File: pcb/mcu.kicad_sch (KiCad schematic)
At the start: 29 parts, among them SW3 TS04-66-50-BK-160-SMT, SW4 PTS645VH58-2 LFS, U1 W25Q128JVS, U2 RP2040, Y1 ABM8AIG-12.000MHZ-12-2Z-T3

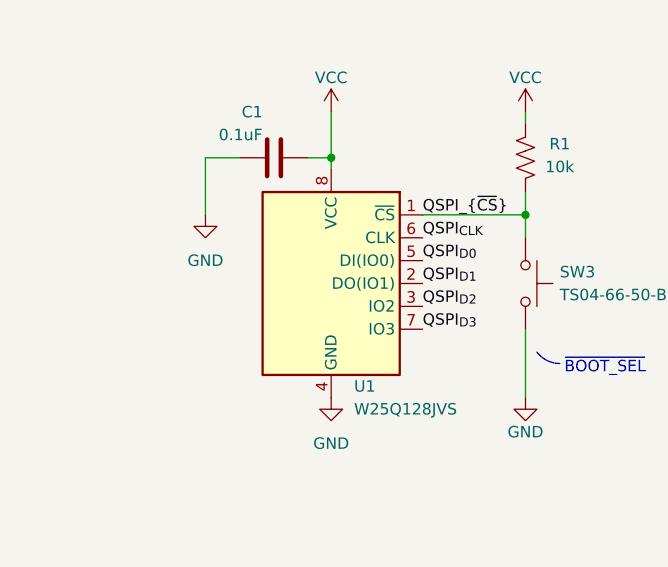
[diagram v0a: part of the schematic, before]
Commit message: Mirror connections on J4
- The schematic presented on OLED datasheet was mirrored commpared to
  the connector's pin order. This fixes that.
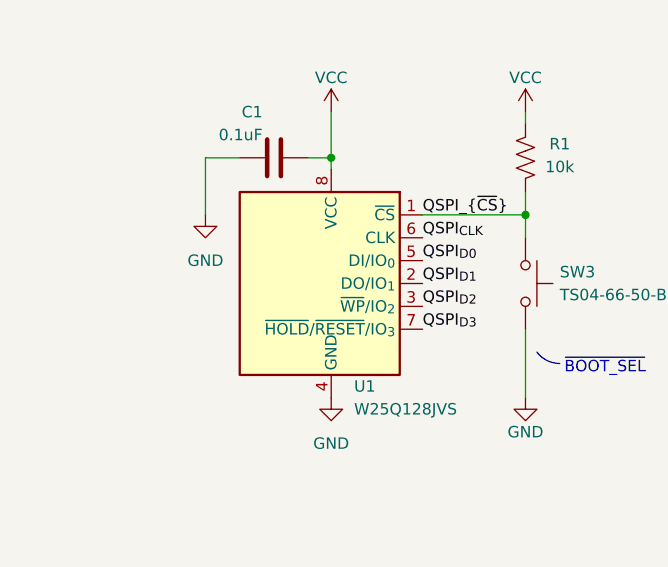
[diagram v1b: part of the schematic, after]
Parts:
- U1: footprint Package_SO:SOIC-8_5.23x5.23mm_P1.27mm -> Package_SO:SOIC-8_5.3x5.3mm_P1.27mm
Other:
- moved on the sheet: U1
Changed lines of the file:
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@@
 (kicad_sch
-	(version 20241209)
+	(version 20250114)
 	(generator "eeschema")
 	(generator_version "9.0")
@@
 			"nn16oXsDE20RirS9sXGrXrG8QahA26gnrKx6yKyjqfMThfpcLvLjw/96ztAkpkKhUCgUCoVCoVDe"
 			"hSbbFAqFQqFQKBRKM0GTbQqFQqFQKBQKpZmgyTaFQqFQKBQKhdIsAP8fPZc3Zc/CT3kAAAAASUVO"
-			"RK5CYII="
+			"RK5CYII+kq/zbaBrasnqHXUbrYl6+ysVTXQyt0RP0+ZJChuDimYnmFv2hKnMoK8GvW69YWXRsES7"
+			"2WgtMpXnE+QgX/4MjazjXZSgoWeKnn16oXsDE20RirS9sXGrXrG8QahA26gnrKx6yKyjqfMThfpc"
+			"LvLjw/96ztAkpkKhUCgUCoVCoVDehSbbFAqFQqFQKBRKM0GTbQqFQqFQKBQKpZmgyTaFQqFQKBQK"
+			"hdIsAP8fPZc3Zc/CT3kAAAAASUVORK5CYIIrAEIAWAAzAFQAQQBvADMALwB6AHIAWQBBADIAUgBH"
+			"AEgAYwBUAFIAdABBAEwANgBjADYAUQBoAE4AMABYAFoAdwBYACsAQgBPAGMAQgBDAHUAUAAzAGsA"
+			"TgBvAFoAbwBoADcARgB6AGMATQBkAHgAUQA2AGkAWgBTAFQAYwBWAEMAdABaAGEAMQBUADgAdABp"
+			"AG4AZwBXAFcAdgBEAEsANgA5ADcAYQBBAHcANQBqAFIAcwBOAEgAdABJAHYAbABqAGEAVwAvAGkA"
+			"OABmAGUAZQBJAEEAagBHAC8AaABlAFQAcABEAHUAOABGAFIAcgAvAG4AVwAwACsAVQBnAEoALwB4"
+			"AGEAbAA3AHgAWgBBAE0AUAB6AHAAdQBsAEQAVgBoAE8ATQBnAEoAYgBpAE4ATQBvAFUAcABsADQA"
+			"TwBMACsAVQAzAGoAdAA4AEYAOQBNAEgAYwB5ADAAQQBqADgASgAvAHIAOABFAGcAKwAyACsAQwBP"
+			"ADUAOQBKAFgAZABDAEYAZQBaAGQAdwB4AEgAZgBCAEoAagBNAG0AZwBtADkAbQBQADAANABkAGIA"
+			"OABMAEgARwBaAC8AaQBWAEYAMQBCADQAYwBnAEgAUwBIADcAVAB5AEMAYQBaAFkAZQBaAEMAOABa"
+			"AEMAVAA3AFMAWQBtADQAbgBiAEEAUQBHADQALwByAFEASQBjAGwAcgBtAEcARAA3AHUARQAzAHkA"
+			"ZwBLADQAbgBFAHgAagBRADIAQgBsAHEAagBxAGQALwBaAGIAcQByAHYAUgBPAFAAeQA4AE4ARQAw"
+			"AEQAUABoAHkASgBoAHoARgBRAFMAWAArAEEANgBSAGMARABjAEwAbAAyAE8AYwBvADUAVwBqAEIA"
+			"WQBwAGcAYgB4AHQAagBvAGcASgBrAHgAVwBxAFgAUgAzADkAawBXAHoAMABXAG4AYwBFADgAeQBV"
+			"AFkASQBsAHgANABHAHkAcABpAEUARwBPAGIAbABoAGgASwBrAHEAUABXADgAMABFAE8AOAAwAFkA"
+			"VQBrAEsAcgBnAFoAZABSAHUAegB6AFUAbgBDADAATABEAEQATQBiAFEAeABzAGQASwBSAHIASgBr"
+			"AEIAKw=="
 		)
 	)
@@
 			"tkw1D4fDwcyZM9G1a1c2RTHNCsApiqIoiqIoimoeeg84RVEURVEURbUiGoBTFEVRFEVRVCuiAThF"
 			"URRFURRFtSIagFMURVEURVFUK6IBOEVRFEVRFEW1IhqAUxRFURRFUVQrogE4RVEURVEURbUa4P8B"
-			"65C3O7MQdOoAAAAASUVORK5CYII="
+			"65C3O7MQdOoAAAAASUVORK5CYILCycwgwMLJzCDEwsnMIMjCycwgzMLJzCDQwsnMINTCycwg2MLJ"
+			"zCDcwsnMIODCycwg5MLJzCDowsnMIOzCycwg8MLJzCD0wsnMIPgCyswg/MLJzCCAw8nMIITDycwg"
+			"iMPJzCCMw8nMIJBDycwglMPJzCCYw8nMIJzDycwgoMPJzCCkw8nMUA6FzdwMzuSMzuwMz/SMz/wM"
+			"2ISN2IwN2ZSN2ZwN2qSN2qwN27SN27wN3MSN3MwN3dSN3dwN3uSN3uwN3/SN3/wN6ISO6IwO6ZSO"
+			"6ZwO6qSO6qwO67SO67wO7MSO7MwO7dSO7dwO7uSO7uwO7/SO7/wO+ISP+IwP+ZSP+ZwP+qSP+qwP"
+			"+7SP+7wP/MSP/MwP/dSP/dwP/uTPDMI6kMwMQTvMILxDycwgwEPJzCDEQ8nMQLhD//jP/8wQyMMM"
+			"wjzQwwxBPcwQ2MMMwT3MEODDDII+7MMMAj+czAxCP5zMDII/nMwMwj+czAwCSJTMDEJIrMwMgkiM"
+			"xAwCSYzEDEJJsMwMgkmUzAzCSZTMDAFKzBCkxAyCSpTMDAFLzBC0xAyBS8xArIQN3RAOzRC8xAwC"
+			"TJTMDFQ+nBAKpZAKrRALtZALvRAMxZAMzRAN1VAO6dAOqc8MgkyUzAzCTJTMDAJNlMwMQU3MENjE"
+			"DEZM9JAP/RAYhdEMwU3MIODEycwg5MTJzCDoRMnMIOzEycwg8ETJzCD0xMnMIPjEycwg/ETJzCCA"
+			"RcnMIITFycwgiMXJzCCMxcnMIJDFycwglMXJzBCYxQzBWcwQoMUMQVrMEKjFDMFazBCwxQxBW8wg"
+			"vAVczCDEhVzMIMwFXcxAuIUe7REfzTAG7MA/IBRCIjRCJFRCJsRDYjRGZFRGZnRGaJRGarRGbNRG"
+			"bvRGcBRHcjRHdFRHdnRHeJRHfTTDoA7740czBHYxQ3AXMwh5UTIzCHpRMjMIe3EyMxB4IUqjREoz"
+			"CHxRMjMIfaEyMwh+oTIzCH+hMjMEoDFDEBozBKIxg1AaJTODYBoqM4NwGiozg4AaJTODkBolM4Og"
+			"Giczg7AaJzNDwBozJKTRSq70SrAUS7I0S7Q0Q9IareRKrwRLsSRLs0RLMySu0Uqu9EqwFEuyNEu0"
+			"NEPyGq3kSq8ES7EkS7NESzMUo1FLtnRLuDSDABslM0MQGzMIslEyMwizUTIzQHUBSqFUSqZ0SqiU"
+			"Sqq0SqyUS7q0S7zUSzMItHEyMwi2oTIzCLehMjMIuFEyMxC1AU7hJE4zCLoxEjMIuzESMwy5QU7l"
+			"NIPAG+I0g9Ab4jSD8BstM4MAHiczgxAeJzODIB4nM4MwHiczg0AeJzODUB4nM4NgHiczg3AeJzOD"
+			"gB4nM4OQHiczg6AeJzODsB4nMw=="
 		)
 	)
@@
 			)
 		)
-		(property "Footprint" "Package_SO:SOIC-8_5.23x5.23mm_P1.27mm"
+		(property "Footprint" "Package_SO:SOIC-8_5.3x5.3mm_P1.27mm"
 			(at 52.07 157.48 0)
 			(effects
@@
 			)
 		)
-		(property "Description" "128Mb Serial Flash Memory, Standard/Dual/Quad SPI, SOIC-8"
+		(property "Description" "128Mbit / 16MiB Serial Flash Memory, Standard/Dual/Quad SPI, 2.7-3.6V, SOIC-8"
 			(at 52.07 157.48 0)
 			(effects

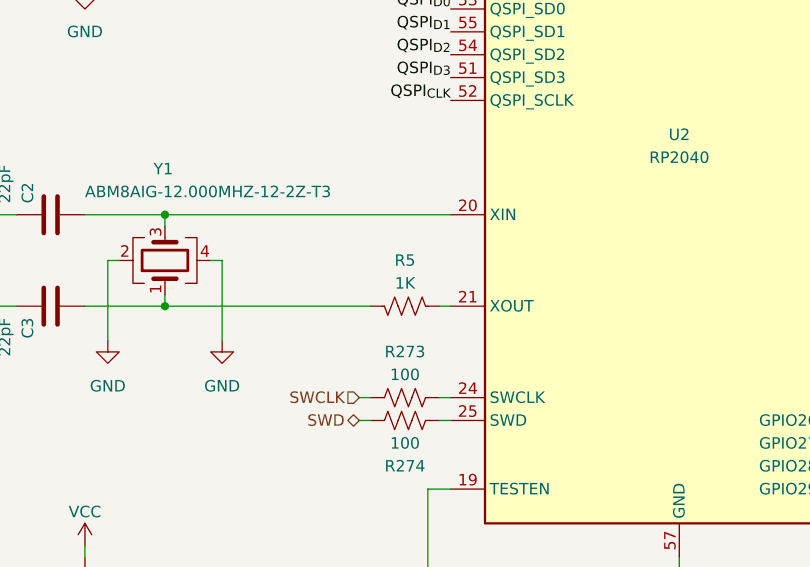
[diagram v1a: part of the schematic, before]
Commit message: Decrease charge indication LED brightness
- 1k current limiting resistor replaced with 4.7k
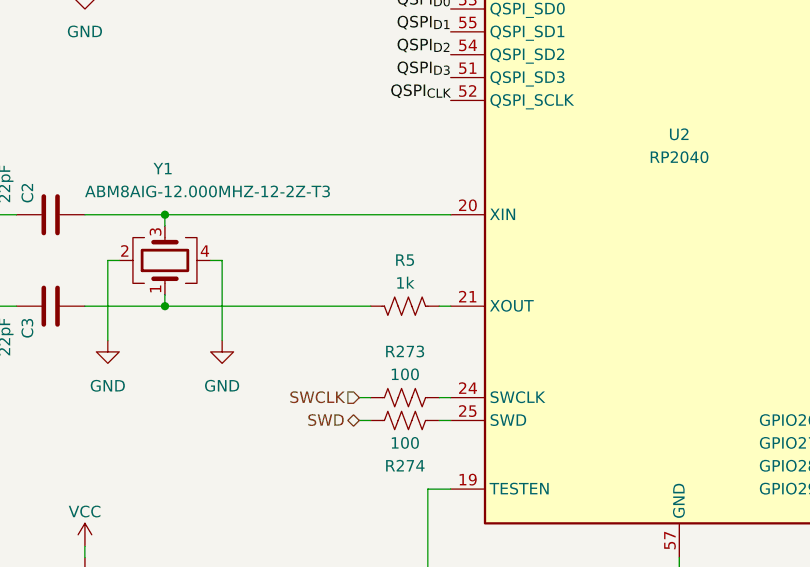
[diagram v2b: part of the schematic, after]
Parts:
- R5: value 1K -> 1k
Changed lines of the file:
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@@
 			)
 		)
-		(property "Value" "1K"
+		(property "Value" "1k"
 			(at 109.22 109.22 90)
 			(effects

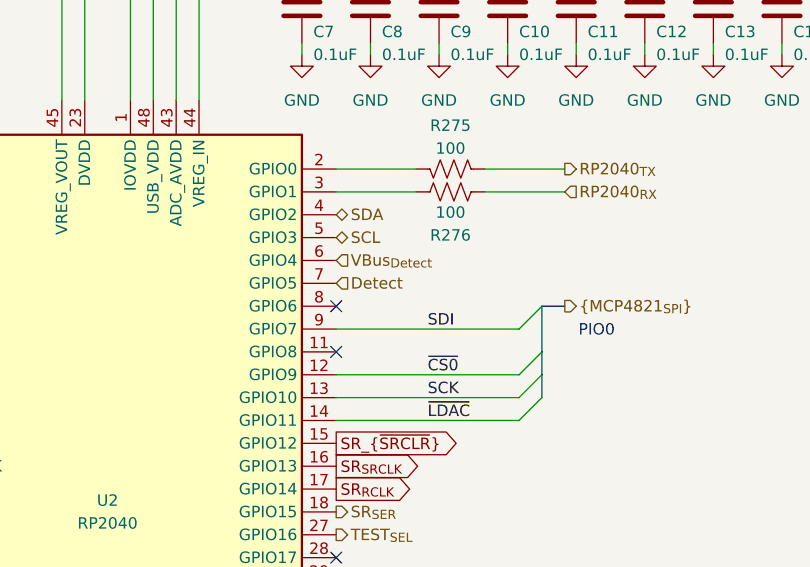
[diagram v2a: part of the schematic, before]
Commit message: Fix electrode coupling
- AC coupling follows attentuation to prevent high-pass filtering
- Remove redundant i2c pullups (can be enabled in MCU if really needed)
- Replace detect line with WP/Detect so that this device can be used to
  program module EEPROM by pulling the line down
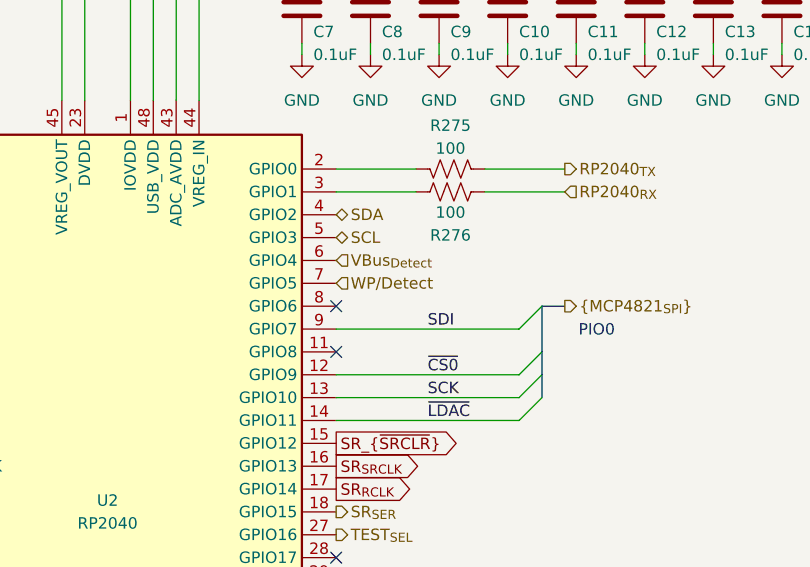
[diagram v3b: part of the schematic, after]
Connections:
- net Detect renamed WP/Detect
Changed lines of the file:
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@@
 			"AFkASQBsAHgANABHAHkAcABpAEUARwBPAGIAbABoAGgASwBrAHEAUABXADgAMABFAE8AOAAwAFkA"
 			"VQBrAEsAcgBnAFoAZABSAHUAegB6AFUAbgBDADAATABEAEQATQBiAFEAeABzAGQASwBSAHIASgBr"
-			"AEIAKw=="
+			"AEIAKwAAAAAAAAAAAAAAAAAAAAAAAAAAAAAAAAAAAAAAAAAAAAAAAAAAAAAAAAAAAAAAAAAAAAAA"
+			"AAAAAAAAAAAAAAAAAAAAAAAAAAAAAAAAAAAAAAAAAAAAAAAAAAAAAAAAAAAAAAAAAAAAAAAAAAAA"
+			"AAAAAAAAAAAAAAAAAAAAAAAAAAAAAAAAAAAAAAAAAAAAAAAAAAAAAAAAAAAAAAAAAAAAAAAAAAAA"
+			"AAAAAAAAAAAAAAAAAAAAAAAAAAAAAAAAAAAAAAAAAAAAAAAAAAAAAAAAAAAAAAAAAAAAAAAAAAAA"
+			"AAAAAAAAAAAAAAAAAAAAAAAAAAAAAAAAAAAAAAAAAAAAAAAAAAAAAAAAAAAAAAAAAAAAAAAAAAAA"
+			"AAAAAAAAAAAAAAAAAAAAAAAAAAAAAAAAAAAAAAAAAAAAAAAAAAAAAAAAAAAAAAAAAAAAAAAAAAAA"
+			"AAAAAAAAAAAAAAAAAAAAAAAAAAAAAAAAAAAAAAAAAAAAAAAAAAAAAAAAAAAAAAAAAAAAAAAAAAAA"
+			"AAAAAAAAAAAAAAAAAAAAAAAAAAAAAAAAAAAAAAAAAAAAAAAAAAAAAAAAAAAAAAAAAAAAAAAAAAAA"
+			"AAAAAAAAAAAAAAAAAAAAAAAAAAAAAAAAAAAAAAAAAAAAAAAAAAAAAAAAAAAAAAAAAAAAAAAAAAAA"
+			"AAAAAAAAAAAAAAAAAAAAAAAAAAAAAAAAAAAAAAAAAAAAAAAAAAAAAAAAAAAAAAAAAAAAAAAAAAAA"
+			"AAAAAAAAAAAAAAAAAAAAAAAAAAAAAAAAAAAAAAAAAAAAAAAAAAAAAAAAAAAAAAAAAAAAAAAAAAAA"
+			"AAAAAAAAAAAAAAAAAAAAAAAAAAAAAAAAAAAAAAAAAAAAAAAAAAAAAAAAAAAAAAAAAAAAAAAAAAAA"
+			"AAAAAAAAAAAAAAAAAAAAAAAAAAAAAAAAAAAAAAAAAAAAAAAAAAAAAAAAAAAAAAAAAAAAAAAAAAAA"
+			"AAAAAAAAAAAAAAAAAAAAAAAAAAAAAAAAAAAAAAAAAAAAAAAAAAAAAAAAAAAAAAAAAAAAAAAAAAAA"
+			"AAAAAAAAAAAAAAAAAAAAAAAAAAAAAAAAAAAAAAAAAAAAAAAAAAAAAAAAAAAAAAAAAAAAAAAAAAAA"
+			"AAAAAAAAAAAAAAAAAAAAAAAAAAAAAAAAAAAAAAAAAAAAAAAAAAAAAAAAAAAAAAAAAAAAAAAAAAAA"
+			"AAAAAAAAAAAAAAAAAAAAAAAAAAAAAAAAAAAAAAAAAAAAAAAAAAAAAAAAAAAAAAAAAAAAAAAAAAAA"
+			"AAAAAAAAAAAAAAAAAAAAAAAAAAAAAAAAAAAAAAAAAAAAAAAAAAAAAAAAAAAAAAAAAAAAAAAAAAAA"
+			"AAAAAA=="
 		)
 	)
@@
 			"Sqq0SqyUS7q0S7zUSzMItHEyMwi2oTIzCLehMjMIuFEyMxC1AU7hJE4zCLoxEjMIuzESMwy5QU7l"
 			"NIPAG+I0g9Ab4jSD8BstM4MAHiczgxAeJzODIB4nM4MwHiczg0AeJzODUB4nM4NgHiczg3AeJzOD"
-			"gB4nM4OQHiczg6AeJzODsB4nMw=="
+			"gB4nM4OQHiczg6AeJzODsB4nMwAAAAAAAAAAAAAAAAAAAAAAAAAAAAAAAAAAAAAAAAAAAAAAAAAA"
+			"AAAAAAAAAAAAAAAAAAAAAAAAAAAAAAAAAAAAAAAAAAAAAAAAAAAAAAAAAAAAAAAAAAAAAAAAAAAA"
+			"AAAAAAAAAAAAAAAAAAAAAAAAAAAAAAAAAAAAAAAAAAAAAAAAAAAAAAAAAAAAAAAAAAAAAAAAAAAA"
+			"AAAAAAAAAAAAAAAAAAAAAAAAAAAAAAAAAAAAAAAAAAAAAAAAAAAAAAAAAAAAAAAAAAAAAAAAAAAA"
+			"AAAAAAAAAAAAAAAAAAAAAAAAAAAAAAAAAAAAAAAAAAAAAAAAAAAAAAAAAAAAAAAAAAAAAAAAAAAA"
+			"AAAAAAAAAAAAAAAAAAAAAAAAAAAAAAAAAAAAAAAAAAAAAAAAAAAAAAAAAAAAAAAAAAAAAAAAAAAA"
+			"AAAAAAAAAAAAAAAAAAAAAAAAAAAAAAAAAAAAAAAAAAAAAAAAAAAAAAAAAAAAAAAAAAAAAAAAAAAA"
+			"AAAAAAAAAAAAAAAAAAAAAAAAAAAAAAAAAAAAAAAAAAAAAAAAAAAAAAAAAAAAAAAAAAAAAAAAAAAA"
+			"AAAAAAAAAAAAAAAAAAAAAAAAAAAAAAAAAAAAAAAAAAAAAAAAAAAAAAAAAAAAAAAAAAAAAAAAAAAA"
+			"AAAAAAAAAAAAAAAAAAAAAAAAAAAAAAAAAAAAAAAAAAAAAAAAAAAAAAAAAAAAAAAAAAAAAAAAAAAA"
+			"AAAAAAAAAAAAAAAAAAAAAAAAAAAAAAAAAAAAAAAAAAAAAAAAAAAAAAAAAAAAAAAAAAAAAAAAAAAA"
+			"AAAAAAAAAAAAAAAAAAAAAAAAAAAAAAAAAAAAAAAAAAAAAAAAAAAAAAAAAAAAAAAAAAAAAAAAAAAA"
+			"AAAAAAAAAAAAAAAAAAAAAAAAAAAAAAAAAAAAAAAAAAAAAAAAAAAAAAAAAAAAAAAAAAAAAAAAAAAA"
+			"AAAAAAAAAAAAAAAAAAAAAAAAAAAAAAAAAAAAAAAAAAAAAAAAAAAAAAAAAAAAAAAAAAAAAAAAAAAA"
+			"AAAAAAAAAAAAAAAAAAAAAAAAAAAAAAAAAAAAAAAAAAAAAAAAAAAAAAAAAAAAAAAAAAAAAAAAAAAA"
+			"AAAAAAAAAAAAAAAAAAAAAAAAAAAAAAAAAAAAAAAAAAAAAAAAAAAAAAAAAAAAAAAAAAAAAAAAAAAA"
+			"AAAAAAAAAAAAAAAAAAAAAAAAAAAAAAAAAAAAAAAAAAAAAAAAAAAAAAAAAAAAAAAAAAAAAAAAAAAA"
+			"AAAAAAAAAAAAAAAAAAAAAAAAAAAAAAAAAAAAAAAAAAAAAAAAAAAAAAAAAAAAAAAAAAAAAAAAAAAA"
+			"AAAAAAAAAAAAAAAAAAAAAAAAAA=="
 		)
 	)
@@
 		)
 	)
-	(hierarchical_label "Detect"
+	(hierarchical_label "WP{slash}Detect"
 		(shape input)
 		(at 165.1 68.58 0)

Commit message: Reduce test signal attenuation
- From -60 dbV to -54 dbV
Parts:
- R275, R276: Tolerance (none) -> 0.1%
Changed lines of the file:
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@@
 			)
 		)
+		(property "Tolerance" ""
+			(at 105.41 63.5 0)
+			(effects
+				(font
+					(size 1.27 1.27)
+				)
+			)
+		)
 		(pin "1"
 		)
@@
 			)
 		)
+		(property "Tolerance" ""
+			(at 184.15 38.1 0)
+			(effects
+				(font
+					(size 1.27 1.27)
+				)
+			)
+		)
 		(pin "1"
 		)
@@
 			)
 		)
+		(property "Tolerance" ""
+			(at 199.39 38.1 0)
+			(effects
+				(font
+					(size 1.27 1.27)
+				)
+			)
+		)
 		(pin "1"
 		)
@@
 			)
 		)
+		(property "Tolerance" ""
+			(at 109.22 121.92 0)
+			(effects
+				(font
+					(size 1.27 1.27)
+				)
+				(hide yes)
+			)
+		)
 		(pin "1"
 		)
@@
 			)
 		)
+		(property "Tolerance" ""
+			(at 214.63 38.1 0)
+			(effects
+				(font
+					(size 1.27 1.27)
+				)
+			)
+		)
 		(pin "1"
 		)
@@
 			)
 		)
+		(property "Tolerance" ""
+			(at 69.85 101.6 0)
+			(effects
+				(font
+					(size 1.27 1.27)
+				)
+			)
+		)
 		(pin "1"
 		)
@@
 			)
 		)
+		(property "Tolerance" ""
+			(at 109.22 124.46 0)
+			(effects
+				(font
+					(size 1.27 1.27)
+				)
+				(hide yes)
+			)
+		)
 		(pin "1"
 		)
@@
 			)
 		)
+		(property "Tolerance" ""
+			(at 207.01 38.1 0)
+			(effects
+				(font
+					(size 1.27 1.27)
+				)
+			)
+		)
 		(pin "1"
 		)
@@
 			)
 		)
+		(property "Tolerance" ""
+			(at 107.95 38.1 0)
+			(effects
+				(font
+					(size 1.27 1.27)
+				)
+			)
+		)
 		(pin "1"
 		)
@@
 			)
 		)
+		(property "Tolerance" ""
+			(at 109.22 111.76 0)
+			(effects
+				(font
+					(size 1.27 1.27)
+				)
+			)
+		)
 		(pin "1"
 		)
@@
 			)
 		)
+		(property "Tolerance" "0.1%"
+			(at 177.8 55.88 0)
+			(effects
+				(font
+					(size 1.27 1.27)
+				)
+				(hide yes)
+			)
+		)
 		(pin "1"
 		)
@@
 			)
 		)
+		(property "Tolerance" ""
+			(at 45.72 143.51 0)
+			(effects
+				(font
+					(size 1.27 1.27)
+				)
+			)
+		)
 		(pin "1"
 		)
@@
 			)
 		)
+		(property "Tolerance" ""
+			(at 124.46 38.1 0)
+			(effects
+				(font
+					(size 1.27 1.27)
+				)
+			)
+		)
 		(pin "1"
 		)
@@
 			)
 		)
+		(property "Tolerance" ""
+			(at 105.41 66.04 0)
+			(effects
+				(font
+					(size 1.27 1.27)
+				)
+			)
+		)
 		(pin "1"
 		)
@@
 			)
 		)
+		(property "Tolerance" ""
+			(at 52.07 157.48 0)
+			(effects
+				(font
+					(size 1.27 1.27)
+				)
+			)
+		)
 		(pin "1"
 		)
@@
 			)
 		)
+		(property "Tolerance" "0.1%"
+			(at 177.8 58.42 0)
+			(effects
+				(font
+					(size 1.27 1.27)
+				)
+				(hide yes)
+			)
+		)
 		(pin "1"
 		)
@@
 			)
 		)
+		(property "Tolerance" ""
+			(at 191.77 38.1 0)
+			(effects
+				(font
+					(size 1.27 1.27)
+				)
+			)
+		)
 		(pin "1"
 		)
@@
 			)
 		)
+		(property "Tolerance" ""
+			(at 222.25 38.1 0)
+			(effects
+				(font
+					(size 1.27 1.27)
+				)
+			)
+		)
 		(pin "1"
 		)
@@
 			)
 		)
+		(property "Tolerance" ""
+			(at 96.52 46.99 0)
+			(effects
+				(font
+					(size 1.27 1.27)
+				)
+			)
+		)
 		(pin "1"
 		)
@@
 			)
 		)
+		(property "Tolerance" ""
+			(at 161.29 38.1 0)
+			(effects
+				(font
+					(size 1.27 1.27)
+				)
+			)
+		)
 		(pin "1"
 		)
@@
 			)
 		)
+		(property "Tolerance" ""
+			(at 73.66 143.51 0)
+			(effects
+				(font
+					(size 1.27 1.27)
+				)
+			)
+		)
 		(pin "1"
 		)
@@
 			)
 		)
+		(property "Tolerance" ""
+			(at 73.66 157.48 0)
+			(effects
+				(font
+					(size 1.27 1.27)
+				)
+			)
+		)
 		(pin "1"
 		)
@@
 			)
 		)
+		(property "Tolerance" ""
+			(at 82.55 106.68 0)
+			(effects
+				(font
+					(size 1.27 1.27)
+				)
+			)
+		)
 		(pin "1"
 		)
@@
 			)
 		)
+		(property "Tolerance" ""
+			(at 73.66 68.58 0)
+			(effects
+				(font
+					(size 1.27 1.27)
+				)
+			)
+		)
 		(pin "1"
 		)
@@
 			)
 		)
+		(property "Tolerance" ""
+			(at 168.91 38.1 0)
+			(effects
+				(font
+					(size 1.27 1.27)
+				)
+			)
+		)
 		(pin "1"
 		)
@@
 			)
 		)
+		(property "Tolerance" ""
+			(at 139.7 93.98 0)
+			(effects
+				(font
+					(size 1.27 1.27)
+				)
+			)
+		)
 		(pin "1"
 		)
@@
 			)
 		)
+		(property "Tolerance" ""
+			(at 116.84 38.1 0)
+			(effects
+				(font
+					(size 1.27 1.27)
+				)
+			)
+		)
 		(pin "1"
 		)
@@
 			)
 		)
+		(property "Tolerance" ""
+			(at 69.85 111.76 0)
+			(effects
+				(font
+					(size 1.27 1.27)
+				)
+			)
+		)
 		(pin "1"
 		)
@@
 			)
 		)
+		(property "Tolerance" ""
+			(at 176.53 38.1 0)
+			(effects
+				(font
+					(size 1.27 1.27)
+				)
+			)
+		)

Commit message: Add SC0914(13) to Part No. field of RP2040
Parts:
- U2: Part No. (none) -> SC0914(13)
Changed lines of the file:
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@@
 			)
 		)
-		(property "Part No." ""
+		(property "Part No." "SC0914(13)"
 			(at 139.7 93.98 0)
 			(effects

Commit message: Rev. C ready for OEPS review
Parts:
- R275, R276: Tolerance 0.1% -> (none)
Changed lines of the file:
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@@
 			"AAAAAAAAAAAAAAAAAAAAAAAAAAAAAAAAAAAAAAAAAAAAAAAAAAAAAAAAAAAAAAAAAAAAAAAAAAAA"
 			"AAAAAAAAAAAAAAAAAAAAAAAAAAAAAAAAAAAAAAAAAAAAAAAAAAAAAAAAAAAAAAAAAAAAAAAAAAAA"
+			"AAAAAAAAAAAAAAAAAAAAAAAAAAAAAAAAAAAAAAAAAAAAAAAAAAAAAAAAAAAAAAAAAAAAAAAAAAAA"
+			"AAAAAAAAAAAAAAAAAAAAAAAAAAAAAAAAAAAAAAAAAAAAAAAAAAAAAAAAAAAAAAAAAAAAAAAAAAAA"
+			"AAAAAAAAAAAAAAAAAAAAAAAAAAAAAAAAAAAAAAAAAAAAAAAAAAAAAAAAAAAAAAAAAAAAAAAAAAAA"
+			"AAAAAAAAAAAAAAAAAAAAAAAAAAAAAAAAAAAAAAAAAAAAAAAAAAAAAAAAAAAAAAAAAAAAAAAAAAAA"
+			"AAAAAAAAAAAAAAAAAAAAAAAAAAAAAAAAAAAAAAAAAAAAAAAAAAAAAAAAAAAAAAAAAAAAAAAAAAAA"
+			"AAAAAAAAAAAAAAAAAAAAAAAAAAAAAAAAAAAAAAAAAAAAAAAAAAAAAAAAAAAAAAAAAAAAAAAAAAAA"
+			"AAAAAAAAAAAAAAAAAAAAAAAAAAAAAAAAAAAAAAAAAAAAAAAAAAAAAAAAAAAAAAAAAAAAAAAAAAAA"
+			"AAAAAAAAAAAAAAAAAAAAAAAAAAAAAAAAAAAAAAAAAAAAAAAAAAAAAAAAAAAAAAAAAAAAAAAAAAAA"
+			"AAAAAAAAAAAAAAAAAAAAAAAAAAAAAAAAAAAAAAAAAAAAAAAAAAAAAAAAAAAAAAAAAAAAAAAAAAAA"
+			"AAAAAAAAAAAAAAAAAAAAAAAAAAAAAAAAAAAAAAAAAAAAAAAAAAAAAAAAAAAAAAAAAAAAAAAAAAAA"
+			"AAAAAAAAAAAAAAAAAAAAAAAAAAAAAAAAAAAAAAAAAAAAAAAAAAAAAAAAAAAAAAAAAAAAAAAAAAAA"
+			"AAAAAAAAAAAAAAAAAAAAAAAAAAAAAAAAAAAAAAAAAAAAAAAAAAAAAAAAAAAAAAAAAAAAAAAAAAAA"
+			"AAAAAAAAAAAAAAAAAAAAAAAAAAAAAAAAAAAAAAAAAAAAAAAAAAAAAAAAAAAAAAAAAAAAAAAAAAAA"
+			"AAAAAAAAAAAAAAAAAAAAAAAAAAAAAAAAAAAAAAAAAAAAAAAAAAAAAAAAAAAAAAAAAAAAAAAAAAAA"
+			"AAAAAAAAAAAAAAAAAAAAAAAAAAAAAAAAAAAAAAAAAAAAAAAAAAAAAAAAAAAAAAAAAAAAAAAAAAAA"
+			"AAAAAAAAAAAAAAAAAAAAAAAAAAAAAAAAAAAAAAAAAAAAAAAAAAAAAAAAAAAAAAAAAAAAAAAAAAAA"
+			"AAAAAAAAAAAAAAAAAAAAAAAAAAAAAAAAAAAAAAAAAAAAAAAAAAAAAAAAAAAAAAAAAAAAAAAAAAAA"
+			"AAAAAAAAAAAAAAAAAAAAAAAAAAAAAAAAAAAAAAAAAAAAAAAAAAAAAAAAAAAAAAAAAAAAAAAAAAAA"
 			"AAAAAA=="
 		)
@@
 			"AAAAAAAAAAAAAAAAAAAAAAAAAAAAAAAAAAAAAAAAAAAAAAAAAAAAAAAAAAAAAAAAAAAAAAAAAAAA"
 			"AAAAAAAAAAAAAAAAAAAAAAAAAAAAAAAAAAAAAAAAAAAAAAAAAAAAAAAAAAAAAAAAAAAAAAAAAAAA"
+			"AAAAAAAAAAAAAAAAAAAAAAAAAAAAAAAAAAAAAAAAAAAAAAAAAAAAAAAAAAAAAAAAAAAAAAAAAAAA"
+			"AAAAAAAAAAAAAAAAAAAAAAAAAAAAAAAAAAAAAAAAAAAAAAAAAAAAAAAAAAAAAAAAAAAAAAAAAAAA"
+			"AAAAAAAAAAAAAAAAAAAAAAAAAAAAAAAAAAAAAAAAAAAAAAAAAAAAAAAAAAAAAAAAAAAAAAAAAAAA"
+			"AAAAAAAAAAAAAAAAAAAAAAAAAAAAAAAAAAAAAAAAAAAAAAAAAAAAAAAAAAAAAAAAAAAAAAAAAAAA"
+			"AAAAAAAAAAAAAAAAAAAAAAAAAAAAAAAAAAAAAAAAAAAAAAAAAAAAAAAAAAAAAAAAAAAAAAAAAAAA"
+			"AAAAAAAAAAAAAAAAAAAAAAAAAAAAAAAAAAAAAAAAAAAAAAAAAAAAAAAAAAAAAAAAAAAAAAAAAAAA"
+			"AAAAAAAAAAAAAAAAAAAAAAAAAAAAAAAAAAAAAAAAAAAAAAAAAAAAAAAAAAAAAAAAAAAAAAAAAAAA"
+			"AAAAAAAAAAAAAAAAAAAAAAAAAAAAAAAAAAAAAAAAAAAAAAAAAAAAAAAAAAAAAAAAAAAAAAAAAAAA"
+			"AAAAAAAAAAAAAAAAAAAAAAAAAAAAAAAAAAAAAAAAAAAAAAAAAAAAAAAAAAAAAAAAAAAAAAAAAAAA"
+			"AAAAAAAAAAAAAAAAAAAAAAAAAAAAAAAAAAAAAAAAAAAAAAAAAAAAAAAAAAAAAAAAAAAAAAAAAAAA"
+			"AAAAAAAAAAAAAAAAAAAAAAAAAAAAAAAAAAAAAAAAAAAAAAAAAAAAAAAAAAAAAAAAAAAAAAAAAAAA"
+			"AAAAAAAAAAAAAAAAAAAAAAAAAAAAAAAAAAAAAAAAAAAAAAAAAAAAAAAAAAAAAAAAAAAAAAAAAAAA"
+			"AAAAAAAAAAAAAAAAAAAAAAAAAAAAAAAAAAAAAAAAAAAAAAAAAAAAAAAAAAAAAAAAAAAAAAAAAAAA"
+			"AAAAAAAAAAAAAAAAAAAAAAAAAAAAAAAAAAAAAAAAAAAAAAAAAAAAAAAAAAAAAAAAAAAAAAAAAAAA"
+			"AAAAAAAAAAAAAAAAAAAAAAAAAAAAAAAAAAAAAAAAAAAAAAAAAAAAAAAAAAAAAAAAAAAAAAAAAAAA"
+			"AAAAAAAAAAAAAAAAAAAAAAAAAAAAAAAAAAAAAAAAAAAAAAAAAAAAAAAAAAAAAAAAAAAAAAAAAAAA"
+			"AAAAAAAAAAAAAAAAAAAAAAAAAAAAAAAAAAAAAAAAAAAAAAAAAAAAAAAAAAAAAAAAAAAAAAAAAAAA"
+			"AAAAAAAAAAAAAAAAAAAAAAAAAAAAAAAAAAAAAAAAAAAAAAAAAAAAAAAAAAAAAAAAAAAAAAAAAAAA"
 			"AAAAAAAAAAAAAAAAAAAAAAAAAA=="
 		)
@@
 			)
 		)
-		(property "Tolerance" "0.1%"
+		(property "Tolerance" ""
 			(at 177.8 55.88 0)
 			(effects
@@
 			)
 		)
-		(property "Tolerance" "0.1%"
+		(property "Tolerance" ""
 			(at 177.8 58.42 0)
 			(effects
